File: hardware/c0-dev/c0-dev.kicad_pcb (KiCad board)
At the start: 2 copper layers, 160 x 68 mm, 455 parts, among them J101 2913730000, J102 2913730000, J103 2913730000, J104 2913730000, J105 2913730000, J106 2913730000, J107 2913730000, J108 2913730000, J109 2913730000, J110 2913730000, J111 2913730000, J112 2913730000, J201 RJ45_LED_Shielded, J401 TAG_CONNECT, J402 PinHeader_2.54mm, Q1001 BSS138P, Q1002 BSS138P, Q1003 BSS138P, Q1004 BSS138P, Q1005 BSS138P, Q1006 BSS138P, Q1007 BSS138P, Q1008 BSS138P, Q1009 BSS138P, Q701 BSS138P, Q702 BSS138P, U1001 TCA9555PWR, U1002 TPS4H000A-Q1, U1003 TPS4H000A-Q1, U1101 LM5160A, U1102 LM317L, U1301 TPS4H000A-Q1, U201 LAN8720A, U301 AP63203WU, U302 TPS2378, U303 TPS54360DDA, U304 TLP175A, U401 TCA9555PWR, U402 W25Q128JVP, U403 RP2350A, U404 TPS3820-33DBV, U501 B0505S-1WR3, U502 ISO1540, U503 ISO1540, U504 TMP117xxDRV, U505 AMS1117-3.3, U506 TMP117xxDRV, U507 ADS1015IDGS, U508 ADS1015IDGS, U601 ADS1015IDGS, U602 ADS1015IDGS, U603 ADS1015IDGS, U604 ADS1015IDGS, U701 B0505S-1WR3, U702 ISO6741, U703 ISO6741, U704 ADS1220xPW, U705 ADS1220xPW, U801 B0505S-1WR3, U802 ISO1044BD, U803 TLP175A, U901 ISO1212, U902 ISO1212, U903 ISO1212, U904 ISO1212, Y401 ABM8-272-T3 (12Mhz)

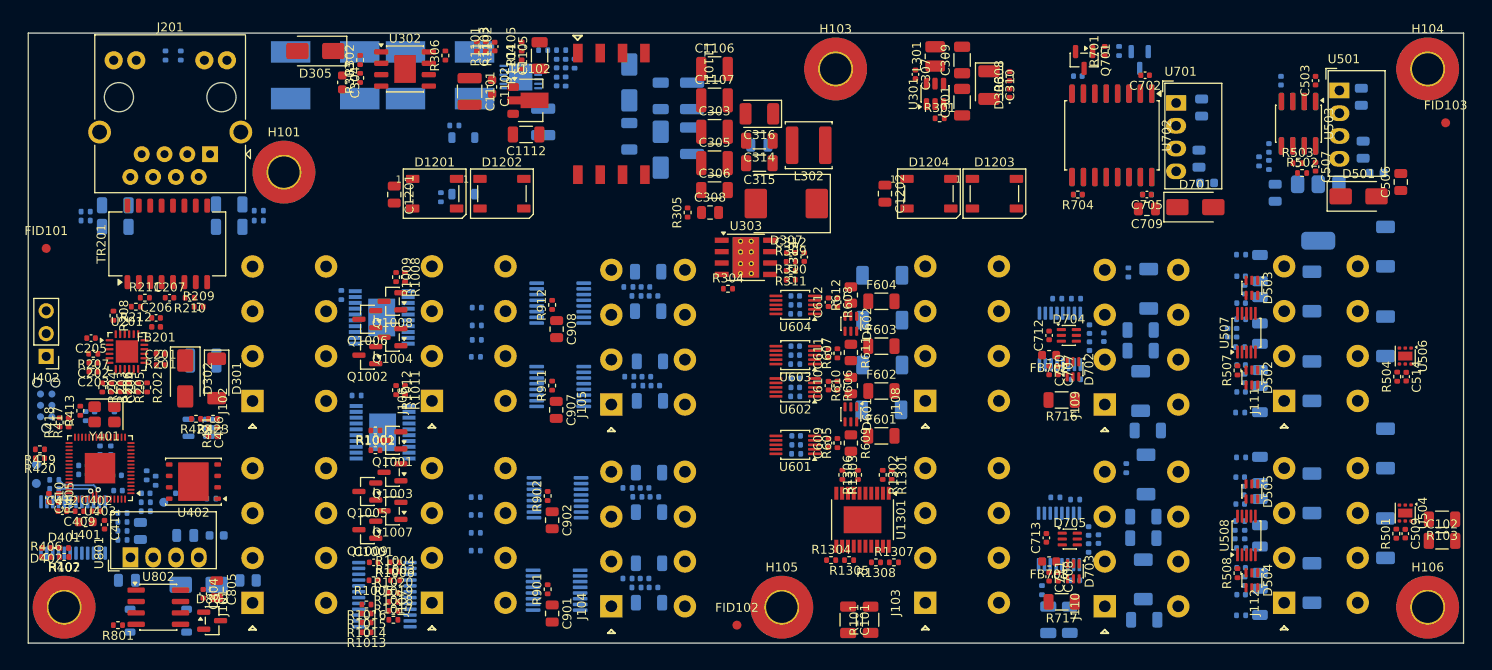
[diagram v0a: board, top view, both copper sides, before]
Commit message: silkscreen, isolation and placement cleanup
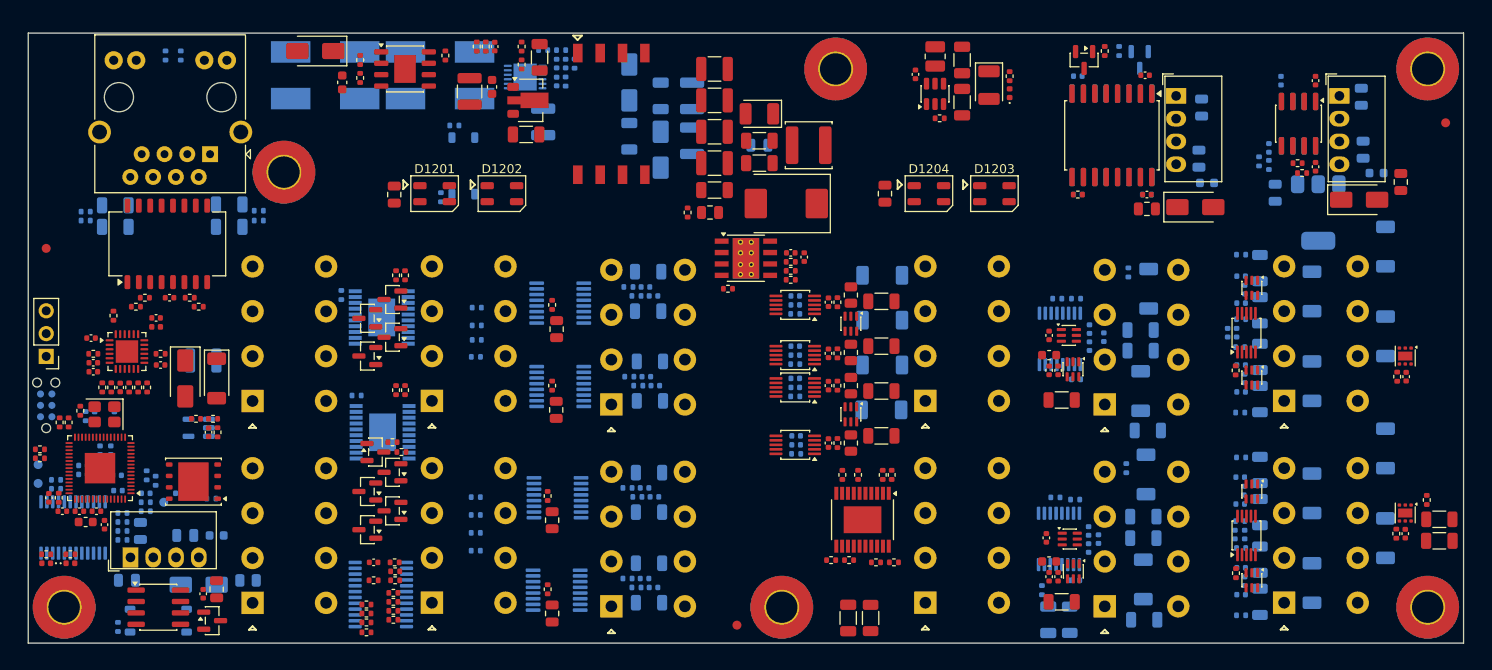
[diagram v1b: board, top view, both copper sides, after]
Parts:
- added R525: 0, Resistor_SMD:R_0402_1005Metric, F.Cu at (215.9, 114.0)
- D1201, D1202, D1203, D1204: footprint LED_SMD:LED_WS2812B_PLCC4_5.0x5.0mm_P3.2mm -> conduit:LED_WS2812B-Mini_PLCC4_3.5x3.5mm
- R801: moved to B.Cu
- moved R1002 3.76 mm to (101.6, 108.7), turned to 0 degrees
- moved D402 3.19 mm to (64.7, 121.1), turned to 0 degrees
- moved R406 2.72 mm to (64.7, 120.1), turned to 180 degrees
- moved D401 2.62 mm to (62.0, 121.1), turned to 180 degrees
- moved Q1001 2.30 mm to (98.7, 108.7), turned to 0 degrees
- moved R1001 2.10 mm to (100.6, 107.6), turned to 180 degrees
- moved R407 2.02 mm to (62.0, 120.1), turned to 0 degrees
- moved U701 0.79 mm to (188.0, 69.0)
- moved U501 0.61 mm to (206.2, 69.0)
- moved U1101 0.49 mm to (115.4, 66.9)
- moved U1001 0.40 mm to (99.3, 124.6)
- moved D501 0.38 mm to (208.4, 80.6)
- moved C102 0.30 mm to (217.3, 118.6)
- moved R103 0.30 mm to (217.3, 116.2)
- moved R507 0.21 mm to (194.6, 99.6)
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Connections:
- net /EN renamed /EN_DO
- net /FAULT_PWR renamed /~{FLT_PWR}
- net /GND_TC renamed /frontend_temp/GND_TC
- C504 pad 1: unconnected-(C504-Pad1) -> Net-(U501-+Vout)
- C504 pad 2: GND -> /frontend_temp/GND
- C505 pad 1: +3.3V -> /frontend_temp/+3.3V
- C505 pad 2: GND -> /frontend_temp/GND
- C506 pad 2: GND -> /frontend_temp/GND
- C507 pad 1: +3.3V -> /frontend_temp/+3.3V
- C507 pad 2: GND -> /frontend_temp/GND
- C508 pad 1: +3.3V -> /frontend_temp/+3.3V
- C508 pad 2: GND -> /frontend_temp/GND
- C509 pad 1: +3.3V -> /frontend_temp/+3.3V
- C509 pad 2: GND -> /frontend_temp/GND
- C510 pad 1: +3.3V -> /frontend_temp/+3.3V
- C510 pad 2: GND -> /frontend_temp/GND
- C511 pad 1: +3.3V -> /frontend_temp/+3.3V
- C511 pad 2: GND -> /frontend_temp/GND
- C512 pad 1: +3.3V -> /frontend_temp/+3.3V
- C512 pad 2: GND -> /frontend_temp/GND
- C513 pad 1: +3.3V -> /frontend_temp/+3.3V
- C513 pad 2: GND -> /frontend_temp/GND
- C514 pad 1: +3.3V -> /frontend_temp/+3.3V
- C514 pad 2: GND -> /frontend_temp/GND
- C515 pad 2: GND -> /frontend_temp/GND
- C517 pad 2: GND -> /frontend_temp/GND
- C518 pad 2: GND -> /frontend_temp/GND
- C520 pad 2: GND -> /frontend_temp/GND
- C521 pad 2: GND -> /frontend_temp/GND
- C523 pad 2: GND -> /frontend_temp/GND
- C524 pad 2: GND -> /frontend_temp/GND
- C526 pad 2: GND -> /frontend_temp/GND
- D502 pad 1: GND -> /frontend_temp/GND
- D502 pad 2: +3.3V -> /frontend_temp/+3.3V
- D502 pad 4: GND -> /frontend_temp/GND
- D502 pad 5: +3.3V -> /frontend_temp/+3.3V
- D503 pad 1: GND -> /frontend_temp/GND
- D503 pad 2: +3.3V -> /frontend_temp/+3.3V
- D503 pad 4: GND -> /frontend_temp/GND
- D503 pad 5: +3.3V -> /frontend_temp/+3.3V
- D504 pad 1: GND -> /frontend_temp/GND
- D504 pad 2: +3.3V -> /frontend_temp/+3.3V
- D504 pad 4: GND -> /frontend_temp/GND
- D504 pad 5: +3.3V -> /frontend_temp/+3.3V
- D505 pad 1: GND -> /frontend_temp/GND
- D505 pad 2: +3.3V -> /frontend_temp/+3.3V
- D505 pad 4: GND -> /frontend_temp/GND
- D505 pad 5: +3.3V -> /frontend_temp/+3.3V
- D506 pad 2: GND -> /frontend_temp/GND
- D507 pad 1: GND -> /frontend_temp/GND
- D508 pad 2: GND -> /frontend_temp/GND
- D509 pad 1: GND -> /frontend_temp/GND
- D510 pad 2: GND -> /frontend_temp/GND
- D511 pad 1: GND -> /frontend_temp/GND
- D512 pad 2: GND -> /frontend_temp/GND
- D513 pad 1: GND -> /frontend_temp/GND
- D702 pad 3: (no net) -> unconnected-(D702B-K1A2-Pad3)
- D702 pad 4: (no net) -> unconnected-(D702B-A3-Pad4)
- D702 pad 5: (no net) -> unconnected-(D702B-K4-Pad5)
- D703 pad 3: (no net) -> unconnected-(D703B-K1A2-Pad3)
- D703 pad 4: (no net) -> unconnected-(D703B-A3-Pad4)
- D703 pad 5: (no net) -> unconnected-(D703B-K4-Pad5)
- R501 pad 1: +3.3V -> /frontend_temp/+3.3V
- R502 pad 2: +3.3V -> /frontend_temp/+3.3V
- R503 pad 2: +3.3V -> /frontend_temp/+3.3V
- R504 pad 1: GND -> /frontend_temp/GND
- R505 pad 2: +3.3V -> /frontend_temp/+3.3V
- R506 pad 2: +3.3V -> /frontend_temp/+3.3V
- R507 pad 1: GND -> /frontend_temp/GND
- R508 pad 1: +3.3V -> /frontend_temp/+3.3V
- R517 pad 2: +3.3V -> /frontend_temp/+3.3V
- R518 pad 1: GND -> /frontend_temp/GND
- R519 pad 2: +3.3V -> /frontend_temp/+3.3V
- R520 pad 1: GND -> /frontend_temp/GND
- R521 pad 2: +3.3V -> /frontend_temp/+3.3V
- R522 pad 1: GND -> /frontend_temp/GND
- R523 pad 2: +3.3V -> /frontend_temp/+3.3V
- R524 pad 1: GND -> /frontend_temp/GND
- R603 pad 1: /I2C2.SDA -> /MCU/I2C2.SDA
- R604 pad 1: /I2C2.SCL -> /MCU/I2C2.SCL
- U501 pad 3: GND -> /frontend_temp/GND
- U502 pad 2: /frontend_temp/SDA -> /MCU/I2C0.SDA
- U502 pad 3: /frontend_temp/SCL -> /MCU/I2C0.SCL
- U502 pad 5: GND -> /frontend_temp/GND
- U502 pad 8: +3.3V -> /frontend_temp/+3.3V
- U503 pad 2: /frontend_temp/SDA_400K -> /MCU/I2C1.SDA
- U503 pad 3: /frontend_temp/SCL_400K -> /MCU/I2C1.SCL
- U503 pad 5: GND -> /frontend_temp/GND
- U503 pad 8: +3.3V -> /frontend_temp/+3.3V
- U504 pad 2: GND -> /frontend_temp/GND
- U504 pad 5: +3.3V -> /frontend_temp/+3.3V
- U505 pad 1: GND -> /frontend_temp/GND
- U505 pad 2: +3.3V -> /frontend_temp/+3.3V
- U506 pad 2: GND -> /frontend_temp/GND
- U506 pad 5: +3.3V -> /frontend_temp/+3.3V
- U507 pad 3: GND -> /frontend_temp/GND
- U507 pad 8: +3.3V -> /frontend_temp/+3.3V
- U508 pad 3: GND -> /frontend_temp/GND
- U508 pad 8: +3.3V -> /frontend_temp/+3.3V
- U601 pad 10: /I2C2.SCL -> /MCU/I2C2.SCL
- U601 pad 9: /I2C2.SDA -> /MCU/I2C2.SDA
- U602 pad 10: /I2C2.SCL -> /MCU/I2C2.SCL
- U602 pad 9: /I2C2.SDA -> /MCU/I2C2.SDA
- U603 pad 10: /I2C2.SCL -> /MCU/I2C2.SCL
- U603 pad 9: /I2C2.SDA -> /MCU/I2C2.SDA
- U604 pad 10: /I2C2.SCL -> /MCU/I2C2.SCL
- U604 pad 9: /I2C2.SDA -> /MCU/I2C2.SDA
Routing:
- net Net-(U403-USB_DP): track 5.98 -> 0.00 mm, vias 1 -> 0
- net Net-(U403-USB_DM): track 4.65 -> 0.00 mm, vias 1 -> 0

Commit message: added 3d models
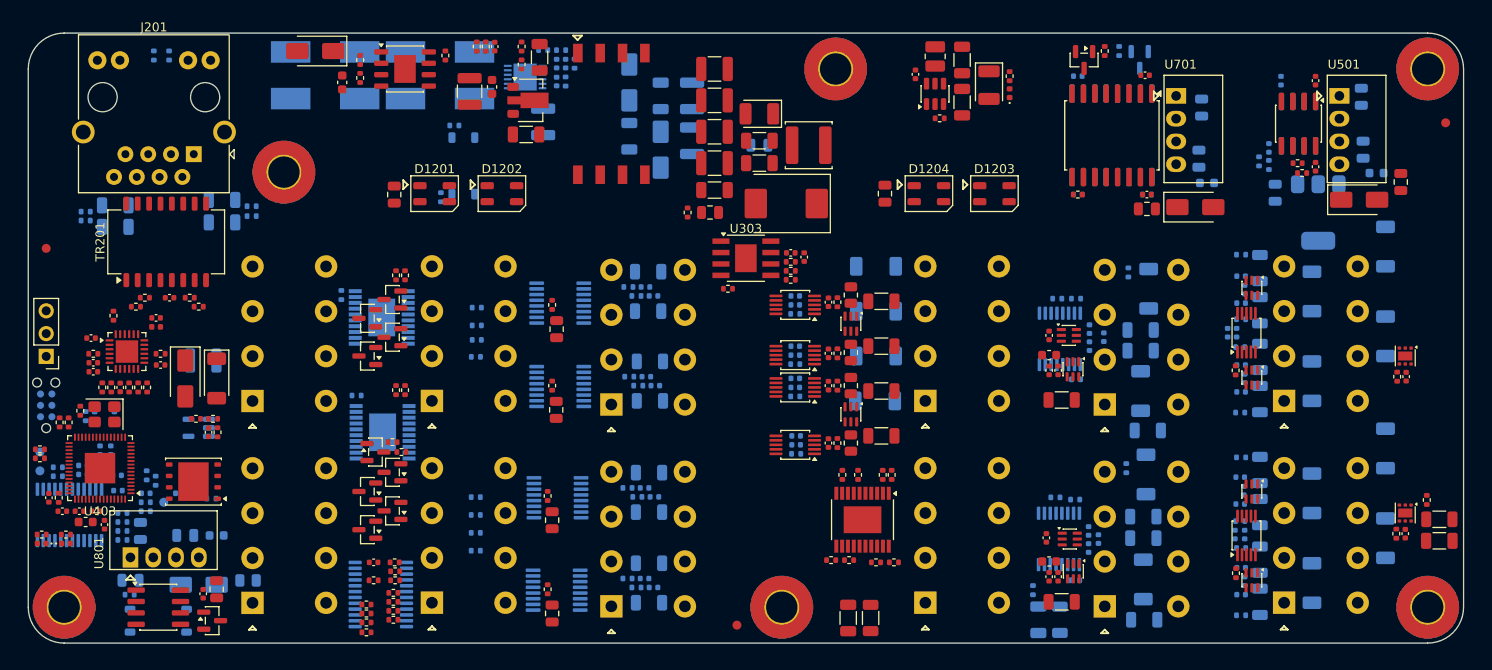
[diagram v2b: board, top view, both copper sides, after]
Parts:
- D303, D304: footprint Diode_SMD:Diode_Bridge_Bourns_CD-DF4xxS -> conduit:Diode_Bridge_Bourns_CD-DF4xxS
- J201: footprint Connector_RJ:RJ45_BEL_SS74301-00x_Vertical -> conduit:RJ45_BEL_SS74301-00x_Vertical
- U303: footprint Package_SO:TI_SO-PowerPAD-8_ThermalVias -> Package_SO:TI_SO-PowerPAD-8
- U403: footprint Package_DFN_QFN:QFN-60-1EP_7x7mm_P0.4mm_EP3.4x3.4mm -> conduit:QFN-60-1EP_7x7mm_P0.4mm_EP3.4x3.4mm
- U501, U701, U801: footprint Converter_DCDC:Converter_DCDC_Murata_MEE1SxxxxSC_THT -> conduit:Converter_DCDC_EVISUN_BXXXXS-1WR3
- moved R801 3.83 mm to (71.3, 124.6), turned to 180 degrees
- moved D401 2.26 mm to (61.5, 118.9)
- moved D402 2.26 mm to (64.2, 118.9)
- moved R406 2.26 mm to (64.2, 117.9)
- moved R407 2.26 mm to (61.5, 117.9)
- moved J201 1.82 mm to (78.5, 75.5)
- moved U401 1.46 mm to (64.6, 115.7)
- moved TP402 1.41 mm to (61.3, 110.8)
- moved R411 1.41 mm to (63.3, 110.4)
- moved R414 1.41 mm to (63.3, 111.4)
- moved TP403 1.41 mm to (61.3, 108.7)
- moved R217 1.30 mm to (75.7, 64.5)
- moved R218 1.30 mm to (74.0, 64.5)
- moved D603 1.22 mm to (154.4, 103.0)
- moved D604 1.22 mm to (154.5, 98.0)
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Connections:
- TR201 pad 12: (no net) -> unconnected-(TR201-NC-Pad12)
- TR201 pad 13: (no net) -> unconnected-(TR201-NC-Pad13)
- TR201 pad 4: (no net) -> unconnected-(TR201-NC-Pad4)
- TR201 pad 5: (no net) -> unconnected-(TR201-NC-Pad5)
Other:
- outline, holes or cut-outs redrawn
